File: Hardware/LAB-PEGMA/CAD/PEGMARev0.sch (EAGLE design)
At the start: 504 parts, among them J12 MINI-USB-UX60A-MB-5ST, J21 D-SUB9-H2M09RA, J41 FTSH-105-02-F-D, J7 Molex 22-28-4030, K1 G6KU-2P-Y, K2 G6KU-2F-Y, K3 G6K-2P, K4 G6K-2G, Q1 2N2222, Q3 2N2222, Q4 2N2222, Q5 2N2222, SW1 B3SN-3012P, SW2 B3SN-3012P, SW3 B3SN-3012P, U1 STM32F205VG, U10 MAX4376, U11 MCP601R, U12 Molex 500873-0816, U13 MAX4376, U14 MAX4376, U15 LM2623, U16 MCP601R, U17 MCP601R, U18 MAX4376, U19 MAX4376, U2 MCP601R, U20 MAX4376, U21 TPS62240DDC, U22 LM2623, U23 MCP601R, U24 MAX4376, U25 MCP601R, U26 MAX4376, U27 MAX4376, U28 LM2623, U29 MCP601R, U3 TPS62240DDC, U30 MAX4376, U31 MAX4376, U32 LM2623, U33 MCP601R, U34 MAX4376, U35 MAX4376, U36 MAX4376, U37 MAX4376, U38 LM2623, U39 MCP601R, U4 MAX4376, U40 LM2623, U41 MAX4376, U42 LM2623, U43 TPS62240DDC, U44 MCP601R, U45 MCP601R, U46 MAX4376, U47 TPS62240DDC, U48 MCP601R, U49 MAX4376, U5 TPS62240DDC, U50 MCP601R, U51 TPS62240DDC, U52 MCP601R, U53 MAX4376, U54 TPS62240DDC, U55 MAX4376, U56 MAX4376, U57 LM2623, U58 HIH6130, U59 25AA512, U6 MCP601R, U60 25AA512, U61 IS61WV51216-10ZSXI, U62 74HC4067, U63 74HC4067, U64 74HC4067, U65 MAX6520, U66 74HC259, U67 MCP601R, U68 ADM3491ARZ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

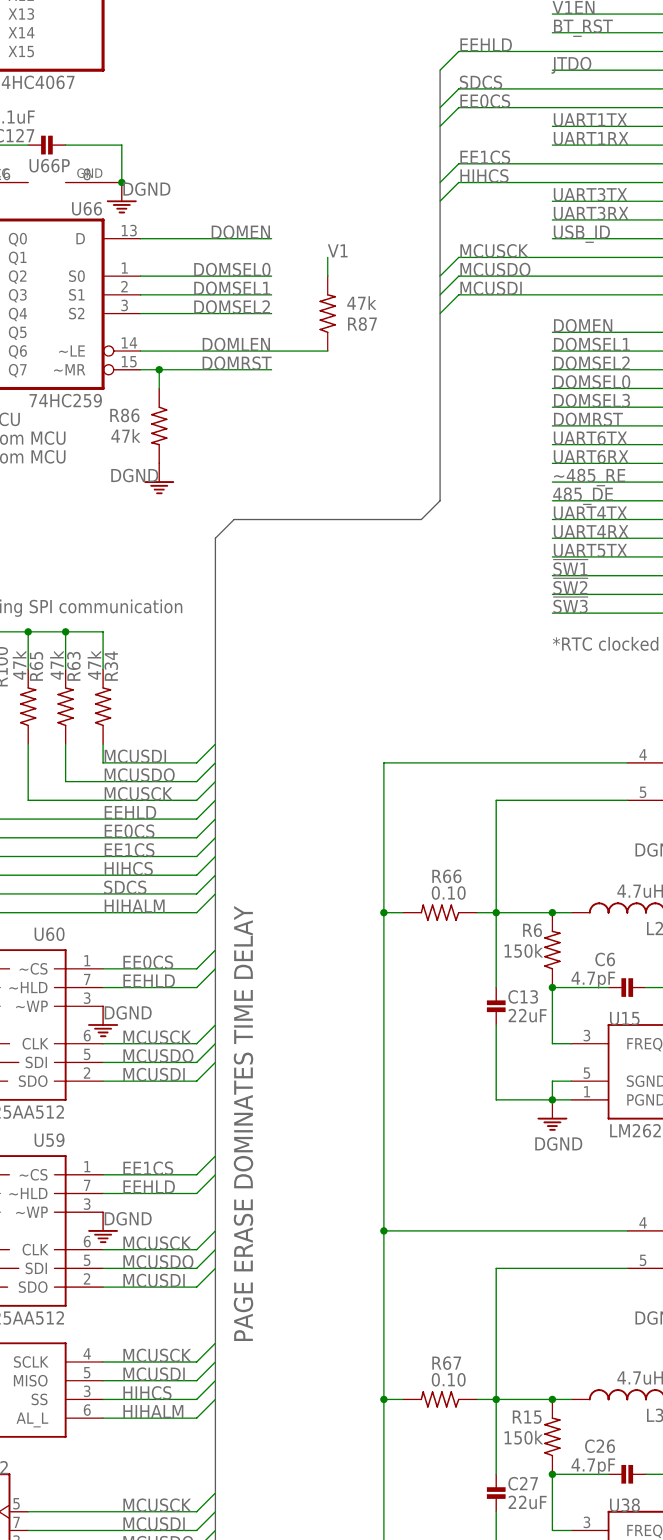
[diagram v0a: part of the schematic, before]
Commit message: adding a note that SPI1 is limited to 15mbps
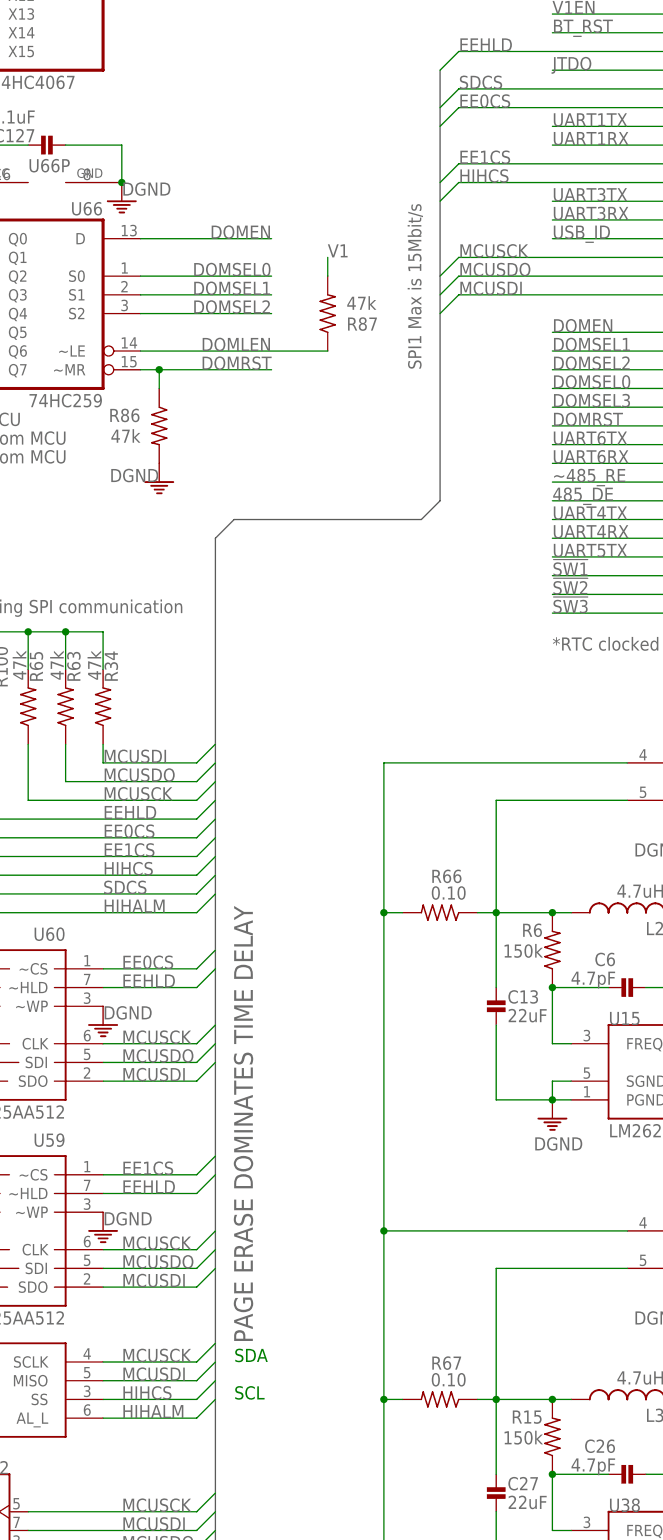
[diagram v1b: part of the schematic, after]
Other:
- note added: "SCL"
- note added: "SDA"
- note added: "SPI1 Max is 15Mbit/s"
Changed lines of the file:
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@@
 <text x="817.88" y="167.64" size="1.778" layer="95">3V - 5.5V</text>
 <text x="812.8" y="241.3" size="1.778" layer="95">Pin13 to VCC per Datasheet</text>
+<text x="457.2" y="114.3" size="1.778" layer="91">SDA</text>
+<text x="457.2" y="109.22" size="1.778" layer="91">SCL</text>
+<text x="482.6" y="248.92" size="1.778" layer="95" rot="R90">SPI1 Max is 15Mbit/s</text>
 </plain>
 <instances>

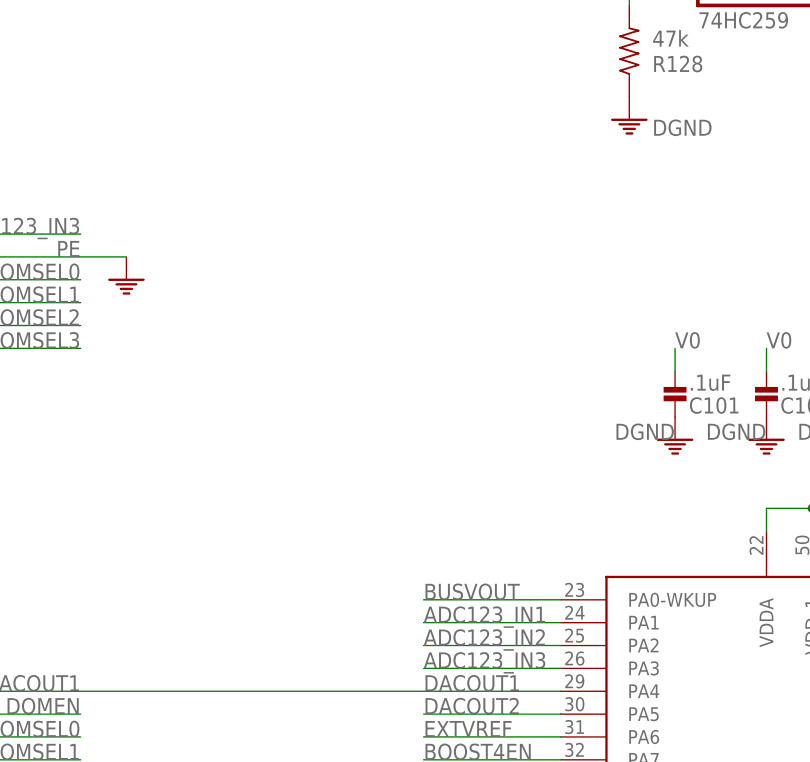
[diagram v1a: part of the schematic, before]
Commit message: 1) Completed ADC DMA transfers 2) Now sampling at 1MHz 3) Added rudimentary retry behavior
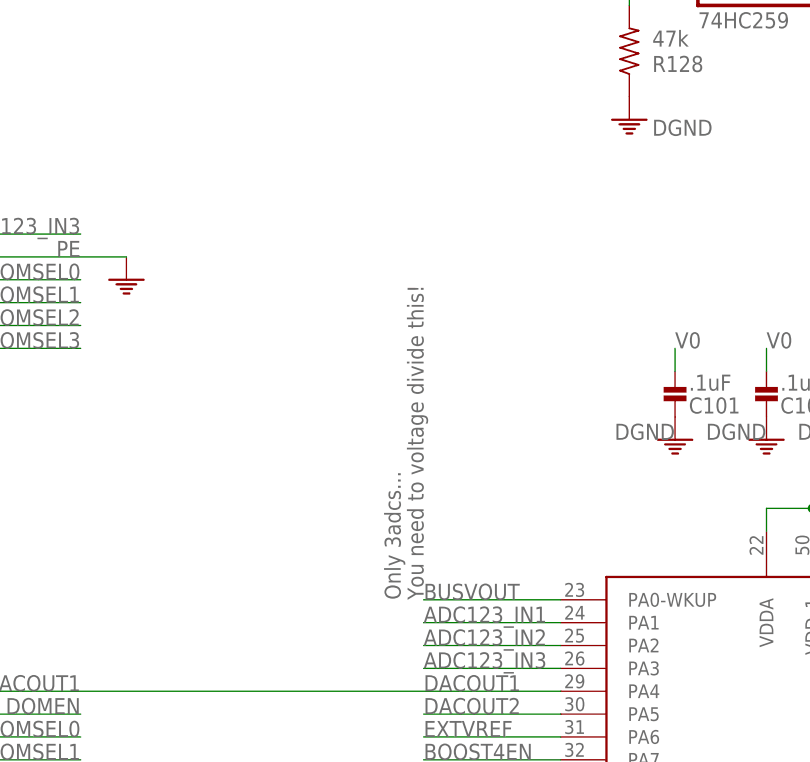
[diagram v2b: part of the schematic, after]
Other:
- note added: "Only 3adcs..."
- note added: "You need to voltage divide this!"
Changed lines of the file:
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@@
 <text x="457.2" y="109.22" size="1.778" layer="91">SCL</text>
 <text x="482.6" y="248.92" size="1.778" layer="95" rot="R90">SPI1 Max is 15Mbit/s</text>
+<text x="500.38" y="340.36" size="1.778" layer="95" rot="R90">You need to voltage divide this!</text>
+<text x="497.84" y="340.36" size="1.778" layer="95" rot="R90">Only 3adcs...</text>
 </plain>
 <instances>

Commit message: Nothing really. Just moved a text line and want to stay up to date
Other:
- note removed: "PAGE ERASE DOMINATES TIME DELAY"
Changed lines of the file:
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@@
 <?xml version="1.0" encoding="utf-8"?>
 <!DOCTYPE eagle SYSTEM "eagle.dtd">
-<eagle version="6.2">
+<eagle version="6.5.0">
 <drawing>
 <settings>
@@
 <text x="782.32" y="25.4" size="6.4516" layer="94">LAB304 LLC</text>
 <text x="848.36" y="5.08" size="5.08" layer="94">0</text>
-<text x="459.74" y="116.84" size="2.54" layer="95" rot="R90">PAGE ERASE DOMINATES TIME DELAY</text>
 <text x="398.78" y="241.3" size="1.778" layer="95">V1EN Controlled from MCU</text>
 <text x="398.78" y="238.76" size="1.778" layer="95">BOOST4EN Controlled from MCU</text>
@@
 <text x="817.88" y="167.64" size="1.778" layer="95">3V - 5.5V</text>
 <text x="812.8" y="241.3" size="1.778" layer="95">Pin13 to VCC per Datasheet</text>
-<text x="457.2" y="114.3" size="1.778" layer="91">SDA</text>
-<text x="457.2" y="109.22" size="1.778" layer="91">SCL</text>
+<text x="457.2" y="116.84" size="1.778" layer="91">SDA</text>
+<text x="457.2" y="111.76" size="1.778" layer="91">SCL</text>
 <text x="482.6" y="248.92" size="1.778" layer="95" rot="R90">SPI1 Max is 15Mbit/s</text>
 <text x="500.38" y="340.36" size="1.778" layer="95" rot="R90">You need to voltage divide this!</text>

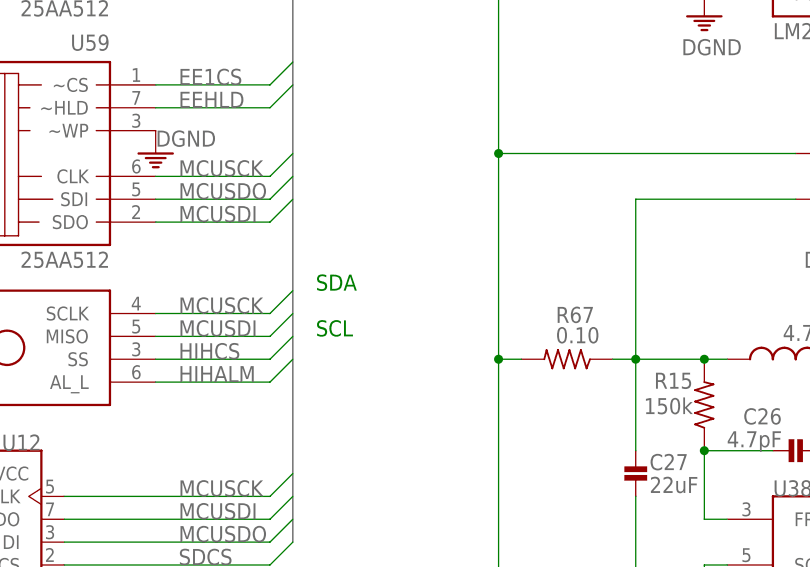
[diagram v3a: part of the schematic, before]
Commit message: These modifications correct the problems encountered with the HIH6130 sensor. There will be further mods, but I wanted to get a working version into the VCS.
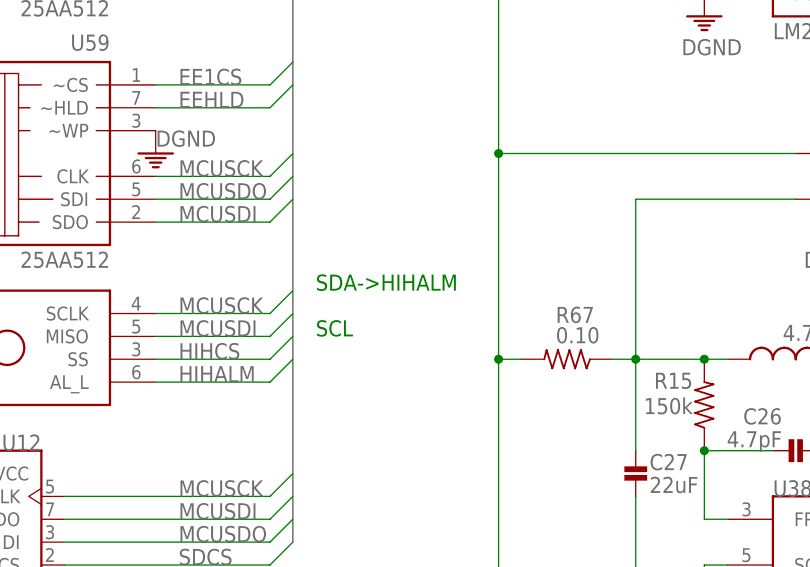
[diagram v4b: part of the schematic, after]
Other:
- note added: "SDA->HIHALM"
- note removed: "SDA"
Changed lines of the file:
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@@
 <text x="817.88" y="167.64" size="1.778" layer="95">3V - 5.5V</text>
 <text x="812.8" y="241.3" size="1.778" layer="95">Pin13 to VCC per Datasheet</text>
-<text x="457.2" y="116.84" size="1.778" layer="91">SDA</text>
+<text x="457.2" y="116.84" size="1.778" layer="91">SDA-&gt;HIHALM</text>
 <text x="457.2" y="111.76" size="1.778" layer="91">SCL</text>
 <text x="482.6" y="248.92" size="1.778" layer="95" rot="R90">SPI1 Max is 15Mbit/s</text>

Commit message: Serial Flash Symbol
Changed the PEGMA board + schematic to reflect the actual serial flash
module populated on it. The board is still rats nested.
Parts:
- removed U59: 25AA512, IKE:25AA512
- added U$5: 25MPX, PEGMA:25MPX
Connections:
- new net HOLD: U$5.~HLD
- new net SF0CS: U$5.~CS
- net EE1CS: no longer U59.~CS
- net EEHLD: no longer U59.~HLD
- net MCUSCK: now also U$5.CLK; no longer U59.CLK
- net MCUSDI: now also U$5.SDO; no longer U59.SDO
- net MCUSDO: now also U$5.SDI; no longer U59.SDI
- net PE: now also U$5.GND, U$5.~WP; no longer U59.GND, U59.~WP
- net V3: now also U$5.VCC; no longer U59.VCC

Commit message: 1) Fixing some inconsistencies that were introduced by changing from an EEPROM symbol to a serial flash symbol
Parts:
- renumbered U$5 to U59
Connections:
- removed net EE1CS: R102.2, U1.PB8
- removed net HOLD: U59.~HLD
- net EEHLD: now also U59.~HLD
- net SF0CS: now also R102.2, U1.PB8
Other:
- moved on the sheet: C17, C45, Y1
